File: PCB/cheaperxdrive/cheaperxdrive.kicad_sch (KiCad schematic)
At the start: 87 parts, among them Q1 JMSL0302AG, Q2 JMSL0302AG, Q3 JMSL0302AG, Q4 JMSL0302AG, Q5 JMSL0302AG, Q6 JMSL0302AG, Q7 JMSL0302AG, Q8 JMSL0302AG, SW1 TS-1187A, U1 STM32F405RGTx, U2 LM5109BMA, U3 DRV8301, U4 AS5047D, U5 SN65HVD232, U6 LP5907MFX-3.3, U7 AMS1117-3.3, Y1 24M

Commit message: finished schematic
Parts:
- added C41, C43, C45: 2u2, symbol Device:C
- added C42, C44, C46: 100n, symbol Device:C
- added D3, D4, D5: DSK310, symbol Device:D_Schottky
- added J1: Screw_Terminal_01x02, symbol Connector:Screw_Terminal_01x02
- added J2: Conn_01x05, Connector_JST:JST_EH_B5B-EH-A_1x05_P2.50mm_Vertical, symbol Connector_Generic:Conn_01x05
- added J3: Conn_01x02, symbol Connector_Generic:Conn_01x02
- added J4: Conn_01x02_Pin, Connector_PinHeader_2.54mm:PinHeader_1x02_P2.54mm_Vertical, symbol Connector:Conn_01x02_Pin
- added J5: Conn_01x05, Connector_JST:JST_EH_B5B-EH-A_1x05_P2.50mm_Vertical, symbol Connector_Generic:Conn_01x06
- added P1: USB_C_Plug_USB2.0, symbol Connector:USB_C_Plug_USB2.0
- added R23, R24, R25, R26, R27, R28: 3k3, symbol Device:R
- added R29: 120, symbol Device:R
- added R30, R31: 5K1, symbol Device:R
- added U10, U8, U9: LM5109BMA, Package_SO:SOIC-8_3.9x4.9mm_P1.27mm, symbol Driver_FET:LM5109BMA
- added U11: L7812, symbol Regulator_Linear:L7812
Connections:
- net +3V3: now also C28.1, U5.3 (VCC), J2.4 (Pin_4)
- net +5V: now also U7.3 (VI)
- net 0GH_A: now also U9.7 (HO)
- net 0GH_B: now also U10.7 (HO)
- net 0GH_C: now also U8.7 (HO)
- net 0GL_A: now also U9.5 (LO)
- net 0GL_B: now also U10.5 (LO)
- net 0GL_C: now also U8.5 (LO)
- net 0SH_A: now also C44.2, U9.6 (HS)
- net 0SH_B: now also C46.2, U10.6 (HS)
- net 0SH_C: now also C42.2, U8.6 (HS)
- net 0SL_B: no longer R8.2
- net 0SL_C: no longer R9.2
- net GND: now also U1.12 (VSSA), U1.18 (VSS), U1.63 (VSS), C41.1, C43.1, C45.1, J1.2 (Pin_2), J2.5 (Pin_5), J5.5 (Pin_5), P1.A1 (GND), P1.A12 (GND), P1.B1 (GND), P1.B12 (GND), P1.S1 (SHIELD), R23.1, R24.1, R25.1, R26.1, R27.1, R28.1, R30.1, R31.1, U10.4 (VSS), U11.2 (GND), U8.4 (VSS), U9.4 (VSS)
- net M0_AH: now also R25.2, U9.2 (HI)
- net M0_AL: now also R26.2, U9.3 (LI)
- net M0_BH: now also R23.2, R27.2, U10.2 (HI), U8.2 (HI)
- net M0_BL: now also R24.2, R28.2, U10.3 (LI), U8.3 (LI)
- net SPI_MISO: now also J5.2 (Pin_2)
- net SPI_MOSI: now also J5.3 (Pin_3)
- net SPI_SCK: now also J5.1 (Pin_1)
- net SWCLK: now also J2.2 (Pin_2)
- net SWDIO: now also J2.3 (Pin_3)
- net USB_N: now also P1.A7 (D-)
- net USB_P: now also P1.A6 (D+)
- net VPP: now also U11.1 (IN)
- net GPIO4: now reaches U1.17 (PA3)
- net SYS_RST: now reaches C24.2, R10.1, SW1.2, U1.7 (NRST)
- net SYS_RST: now also J2.1 (Pin_1)
- net at C26.2, D2.2 (A), U2.1 (VDD): now also C41.2, C43.2, C45.2, D3.2 (A), D4.2 (A), D5.2 (A), U10.1 (VDD), U11.3 (OUT), U8.1 (VDD), U9.1 (VDD)
- net CAN_L: now reaches U5.6 (CANL)
- net CAN_L: now also J3.2 (Pin_2), J4.1 (Pin_1)
- net CAN_H: now reaches U5.7 (CANH)
- net CAN_H: now also J3.1 (Pin_1), R29.2
- new net: C46.1, D5.1 (K), U10.8 (HB)
- new net: J4.2 (Pin_2), R29.1
- new net: C42.1, D3.1 (K), U8.8 (HB)
- new net: C44.1, D4.1 (K), U9.8 (HB)
- new net: P1.A5 (CC), R31.2
- new net: P1.A4 (VBUS), P1.A9 (VBUS), P1.B4 (VBUS), P1.B9 (VBUS)
- new net: P1.B5 (VCONN), R30.2
- new net GPIO6: J5.4 (Pin_4)
- new net S1_N: R8.2
- new net S2_N: R9.2
- new net VDD: J1.1 (Pin_1)
- no-connect marks 27 -> 26
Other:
- note added: "CAN Transciever"
- note added: "Connectors"
- note added: "Gate Driver for bridge"
- note added: "MCU - STM32"
- note added: "Motor Driver"
- note added: "Power Bridge"
- note added: "Rotary Encoder"
- note added: "SWD"
- note added: "Step Down Voltage (to 3.3V and 5V)"
- moved on the sheet: C1, C10, C11, C12, C13, C14, C15, C16, C17, C18, C19, C2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

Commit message: started schematic
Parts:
- removed J1: Screw_Terminal_01x02, symbol Connector:Screw_Terminal_01x02
- added H10, H11, H12, H13, H8, H9: MountingHole, MountingHole:MountingHole_3.2mm_M3, symbol Mechanical:MountingHole
- added H6, H7: MountingHole_Pad, MountingHole:MountingHole_4.3mm_M4_Pad_Via, symbol Mechanical:MountingHole_Pad
- added TP1, TP2, TP3: TestPoint, TestPoint:TestPoint_Pad_D2.5mm, symbol Connector:TestPoint
- added U12: USBLC6-2SC6, Package_TO_SOT_SMD:SOT-23-6, symbol Power_Protection:USBLC6-2SC6
- C1, C10, C11, C12, C13, C14, C15, C16, C17, C18, C19, C2, C20, C21, C22, C23, C24, C25, C26, C27, C28, C29, C3, C30, C31, C32, C38, C39, C4, C40, C41, C42, C43, C44, C45, C46, C5, C6, C7, C8, C9, D1, D2, D3, D4, D5: footprint (none) -> Capacitor_SMD:C_0201_0603Metric
- C33, C34, C35, C36, C37: footprint (none) -> Capacitor_THT:CP_Radial_D5.0mm_P2.50mm
- J3: footprint (none) -> Connector_JST:JST_XH_B2B-XH-AM_1x02_P2.50mm_Vertical
- J5: footprint Connector_JST:JST_EH_B5B-EH-A_1x05_P2.50mm_Vertical -> Connector_JST:JST_EH_B6B-EH-A_1x06_P2.50mm_Vertical
- L1: footprint (none) -> Inductor_SMD:L_0201_0603Metric
- P1: footprint (none) -> Connector_USB:USB_C_Receptacle_HRO_TYPE-C-31-M-12; symbol Connector:USB_C_Plug_USB2.0 -> Connector:USB_C_Receptacle_USB2.0_16P
- R1, R10, R11, R12, R13, R14, R15, R16, R17, R18, R19, R2, R20, R21, R22, R23, R24, R25, R26, R27, R28, R29, R3, R30, R31, R4, R5, R6, R7, R8, R9: footprint (none) -> Resistor_SMD:R_0201_0603Metric
- SW1: footprint (none) -> Button_Switch_SMD:SW_SPST_CK_RS282G05A3
- U11: footprint (none) -> L8712:78XXS; symbol Regulator_Linear:L7812 -> ldo:L7812; Availability (none) -> In Stock; Check_prices (none) -> https://www.snapeda.com/parts/L7812/STMicroelectronics/view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; Description_1 (none) -> Linear Voltage Regulator IC Positive Fixed 1 Output 1.5A TO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; MF (none) -> STMicroelectronics; MP (none) -> L7812; Package (none) -> Package; Price (none) -> None; SnapEDA_Link (none) -> https://www.snapeda.com/parts/L7812/STMicroelectronics/view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
- Y1: footprint (none) -> Crystal:Crystal_SMD_3225-4Pin_3.2x2.5mm
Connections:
- net +3V3: now also TP1.1
- net +5V: now also TP2.1
- net GND: now also U11.GND, H7.1, TP3.1, U12.2 (GND); no longer U11.2 (GND)
- net USB_N: now also P1.B7 (D-), U12.3 (I/O2), U12.4 (I/O2)
- net USB_P: now also P1.B6 (D+), U12.1 (I/O1), U12.6 (I/O1)
- net VDD: now also H6.1
- net VPP: now also U11.IN; no longer U11.1 (IN)
- net at C26.2, C41.2, C43.2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: now also U11.OUT; no longer U11.3 (OUT)
- net USB_VBUS: now reaches P1.A4 (VBUS), P1.A9 (VBUS), P1.B4 (VBUS), P1.B9 (VBUS)
- net USB_VBUS: now also U12.5 (VBUS)
- no-connect marks 26 -> 28

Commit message: finished first layer, may rework
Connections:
- net VDD is gone; now on net VPP: H6.1
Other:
- moved on the sheet: R30
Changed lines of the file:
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@@
 	)
 	(junction
+		(at 355.6 107.95)
+		(diameter 0)
+		(color 0 0 0 0)
+	)
+	(junction
 		(at 64.77 246.38)
 		(diameter 0)
@@
 	)
 	(junction
+		(at 355.6 109.22)
+		(diameter 0)
+		(color 0 0 0 0)
+	)
+	(junction
 		(at 193.04 124.46)
 		(diameter 0)
@@
 	(wire
 		(pts
-			(xy 358.14 109.22) (xy 388.62 109.22)
+			(xy 355.6 109.22) (xy 388.62 109.22)
 		)
 		(stroke
@@
 	(wire
 		(pts
+			(xy 358.14 115.57) (xy 358.14 118.11)
+		)
+		(stroke
+			(width 0)
+			(type default)
+		)
+	)
+	(wire
+		(pts
 			(xy 22.86 58.42) (xy 22.86 60.96)
 		)
@@
 	(wire
 		(pts
-			(xy 355.6 110.49) (xy 355.6 104.14)
+			(xy 355.6 110.49) (xy 355.6 109.22)
 		)
 		(stroke
@@
 	(wire
 		(pts
+			(xy 355.6 115.57) (xy 358.14 115.57)
+		)
+		(stroke
+			(width 0)
+			(type default)
+		)
+	)
+	(wire
+		(pts
 			(xy 64.77 236.22) (xy 64.77 246.38)
 		)
@@
 	(wire
 		(pts
+			(xy 355.6 107.95) (xy 355.6 104.14)
+		)
+		(stroke
+			(width 0)
+			(type default)
+		)
+	)
+	(wire
+		(pts
 			(xy 133.35 246.38) (xy 143.51 246.38)
 		)
@@
 	(wire
 		(pts
-			(xy 358.14 110.49) (xy 358.14 109.22)
+			(xy 355.6 107.95) (xy 355.6 109.22)
 		)
 		(stroke
@@
 			)
 		)
-		(property "Value" "VDD"
-			(at 378.46 78.74 0)
+		(property "Value" "VPP"
+			(at 381 82.5499 0)
 			(effects
 				(font
 					(size 1.27 1.27)
 				)
+				(justify left)
 			)
 		)
@@
 	(symbol
 		(lib_id "Device:R")
-		(at 358.14 114.3 0)
+		(at 355.6 111.76 0)
 		(unit 1)
 		(exclude_from_sim no)
@@
 		(dnp no)
 		(property "Reference" "R30"
-			(at 362.204 107.95 0)
+			(at 359.664 105.41 0)
 			(effects
 				(font
@@
 		)
 		(property "Value" "5K1"
-			(at 362.204 105.41 0)
+			(at 359.664 102.87 0)
 			(effects
 				(font
@@
 		)
 		(property "Footprint" "Resistor_SMD:R_0201_0603Metric"
-			(at 356.362 114.3 90)
+			(at 353.822 111.76 90)
 			(effects
 				(font
@@
 		)
 		(property "Datasheet" "~"
-			(at 358.14 114.3 0)
+			(at 355.6 111.76 0)
 			(effects
 				(font
@@
 		)
 		(property "Description" "Resistor"
-			(at 358.14 114.3 0)
+			(at 355.6 111.76 0)
 			(effects
 				(font

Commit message: new schematic
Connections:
- net S1_N is gone; now on net 0SL_B: R8.2
- net S2_N is gone; now on net 0SL_C: R9.2
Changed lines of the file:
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@@
 	)
 	(junction
+		(at 226.06 201.93)
+		(diameter 0)
+		(color 0 0 0 0)
+	)
+	(junction
 		(at 307.34 222.25)
 		(diameter 0)
@@
 	)
 	(junction
+		(at 266.7 201.93)
+		(diameter 0)
+		(color 0 0 0 0)
+	)
+	(junction
 		(at 124.46 125.73)
 		(diameter 0)
@@
 	(wire
 		(pts
+			(xy 264.16 201.93) (xy 266.7 201.93)
+		)
+		(stroke
+			(width 0)
+			(type default)
+		)
+	)
+	(wire
+		(pts
 			(xy 226.06 219.71) (xy 266.7 219.71)
 		)
@@
 		)
 		(stroke
+			(width 0)
+			(type default)
+		)
+	)
+	(wire
+		(pts
+			(xy 223.52 201.93) (xy 226.06 201.93)
+		)
+		(stroke

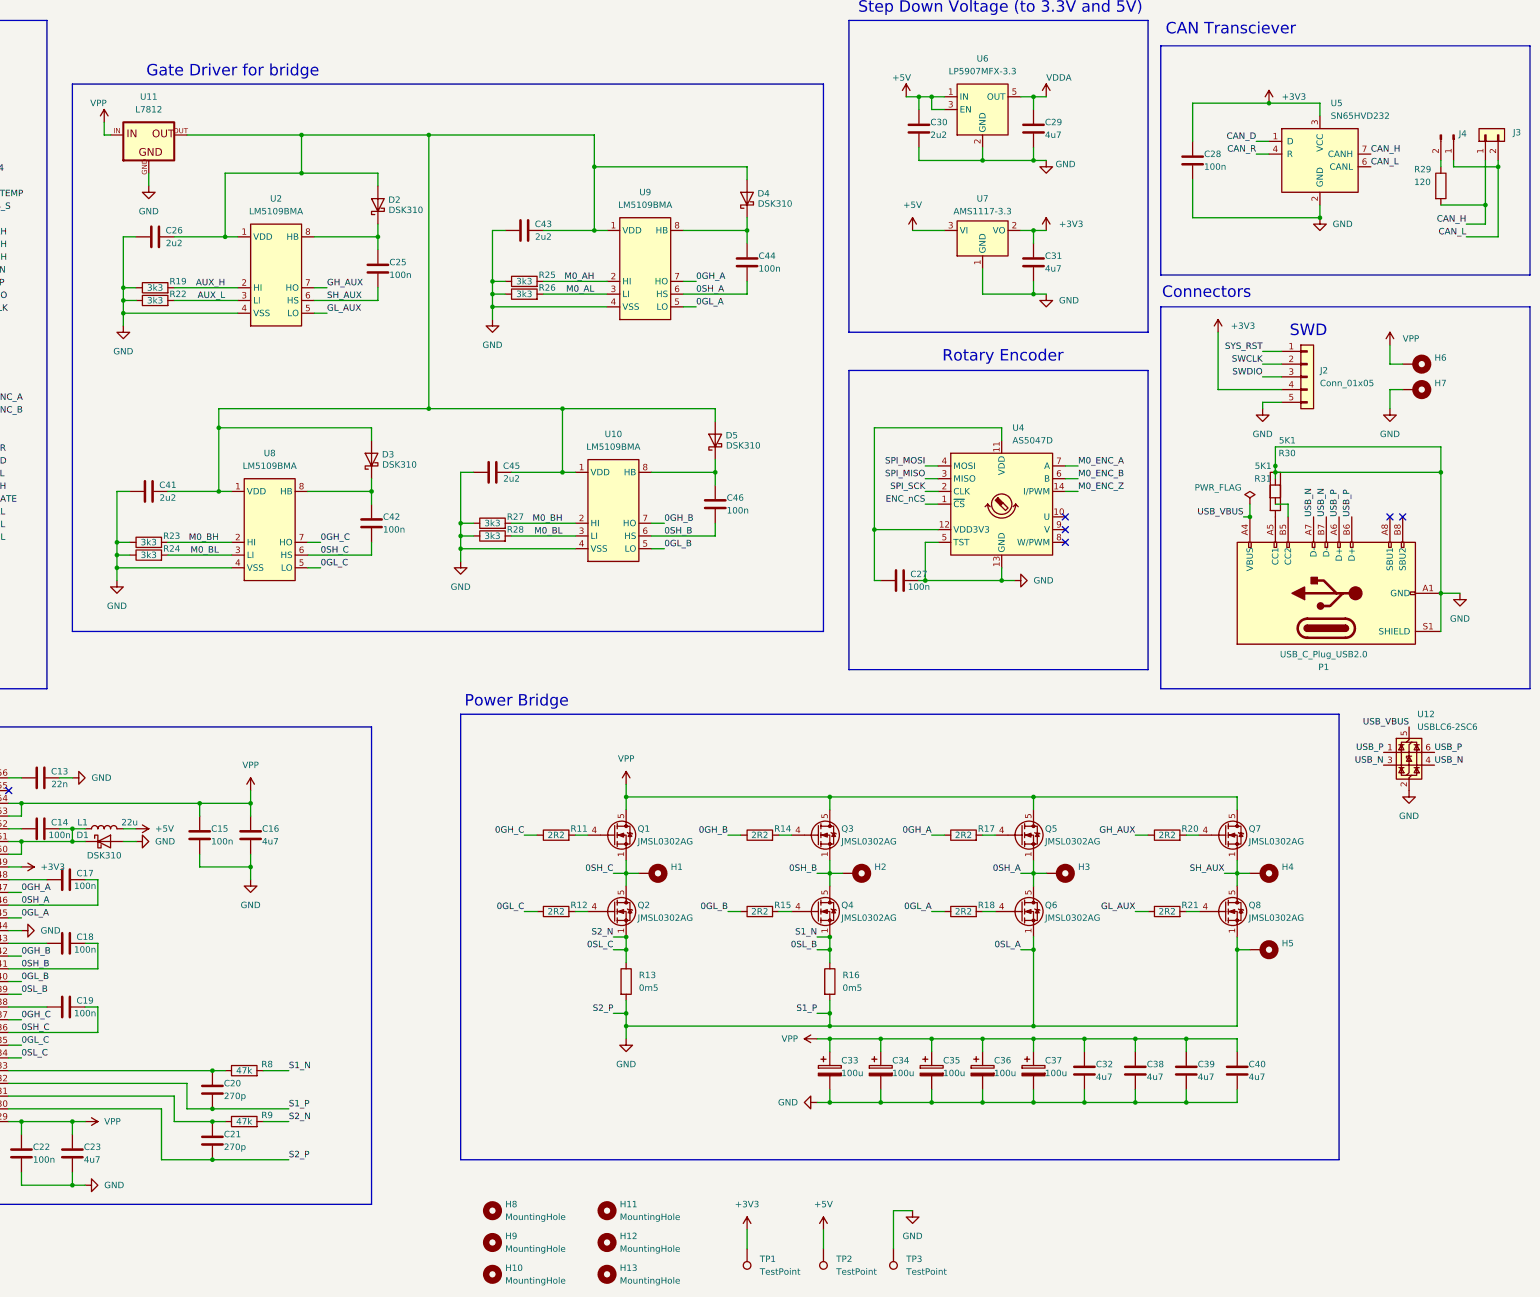
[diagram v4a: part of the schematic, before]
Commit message: pausing pcb work for now, corrected schematic to remove redundant gate drivers and removed 5v ldo
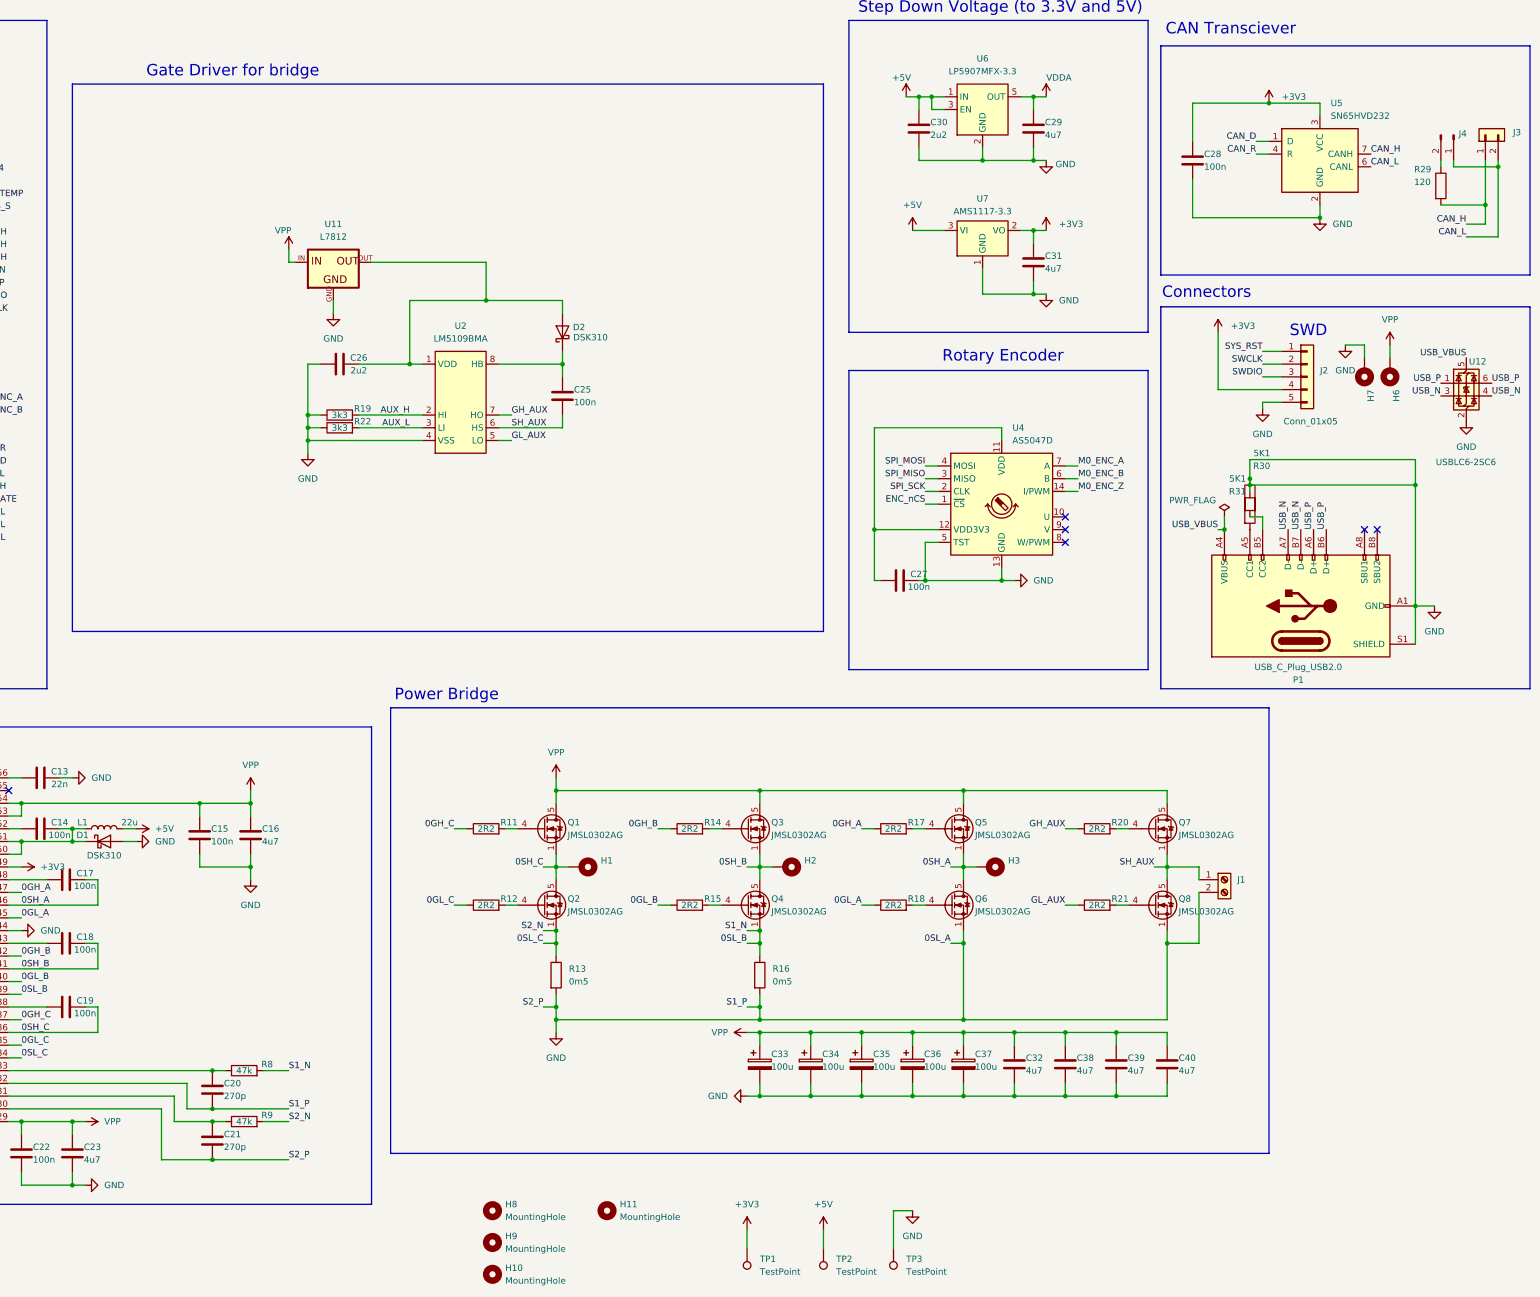
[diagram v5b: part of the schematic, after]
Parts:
- removed C41, C43, C45: 2u2, Capacitor_SMD:C_0201_0603Metric, symbol Device:C
- removed C42, C44, C46: 100n, Capacitor_SMD:C_0201_0603Metric, symbol Device:C
- removed D3, D4, D5: DSK310, Capacitor_SMD:C_0201_0603Metric, symbol Device:D_Schottky
- removed H12, H13: MountingHole, MountingHole:MountingHole_3.2mm_M3, symbol Mechanical:MountingHole
- removed H4, H5: MountingHole_Pad, MountingHole:MountingHole_4.3mm_M4_Pad_Via, symbol Mechanical:MountingHole_Pad
- removed R23, R24, R25, R26, R27, R28: 3k3, Resistor_SMD:R_0201_0603Metric, symbol Device:R
- removed U10, U8, U9: LM5109BMA, Package_SO:SOIC-8_3.9x4.9mm_P1.27mm, symbol Driver_FET:LM5109BMA
- added J1: Screw_Terminal_01x02, TerminalBlock_Phoenix:TerminalBlock_Phoenix_MPT-0,5-2-2.54_1x02_P2.54mm_Horizontal, symbol Connector:Screw_Terminal_01x02
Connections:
- net GND: now also J1.2 (Pin_2)
- net SH_AUX: now also J1.1 (Pin_1)
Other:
- moved on the sheet: C25, C26, C32, C33, C34, C35, C36, C37, C38, C39, C40, D2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
